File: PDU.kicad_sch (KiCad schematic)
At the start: 36 parts, among them Q37 PMOS, Q38 NPN, Q39 NPN, Q40 PMOS, Q41 NPN, Q42 PMOS, Q43 NPN, Q44 PMOS, Q45 NPN, Q46 PMOS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

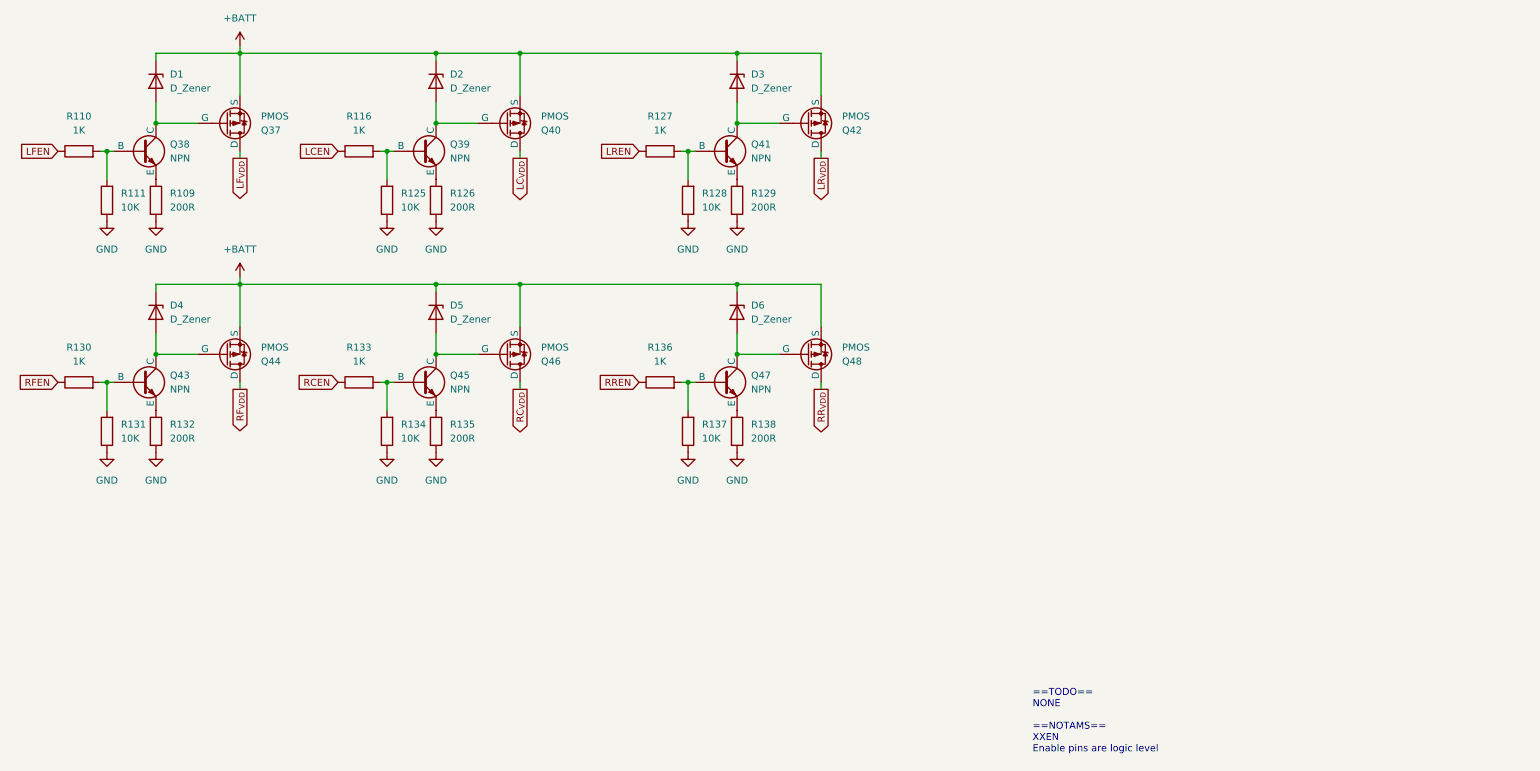
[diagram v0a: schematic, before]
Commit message: The great decluttering
Moved all possible controls to I2C, part selection commenced, IOs assigned pending comms schema
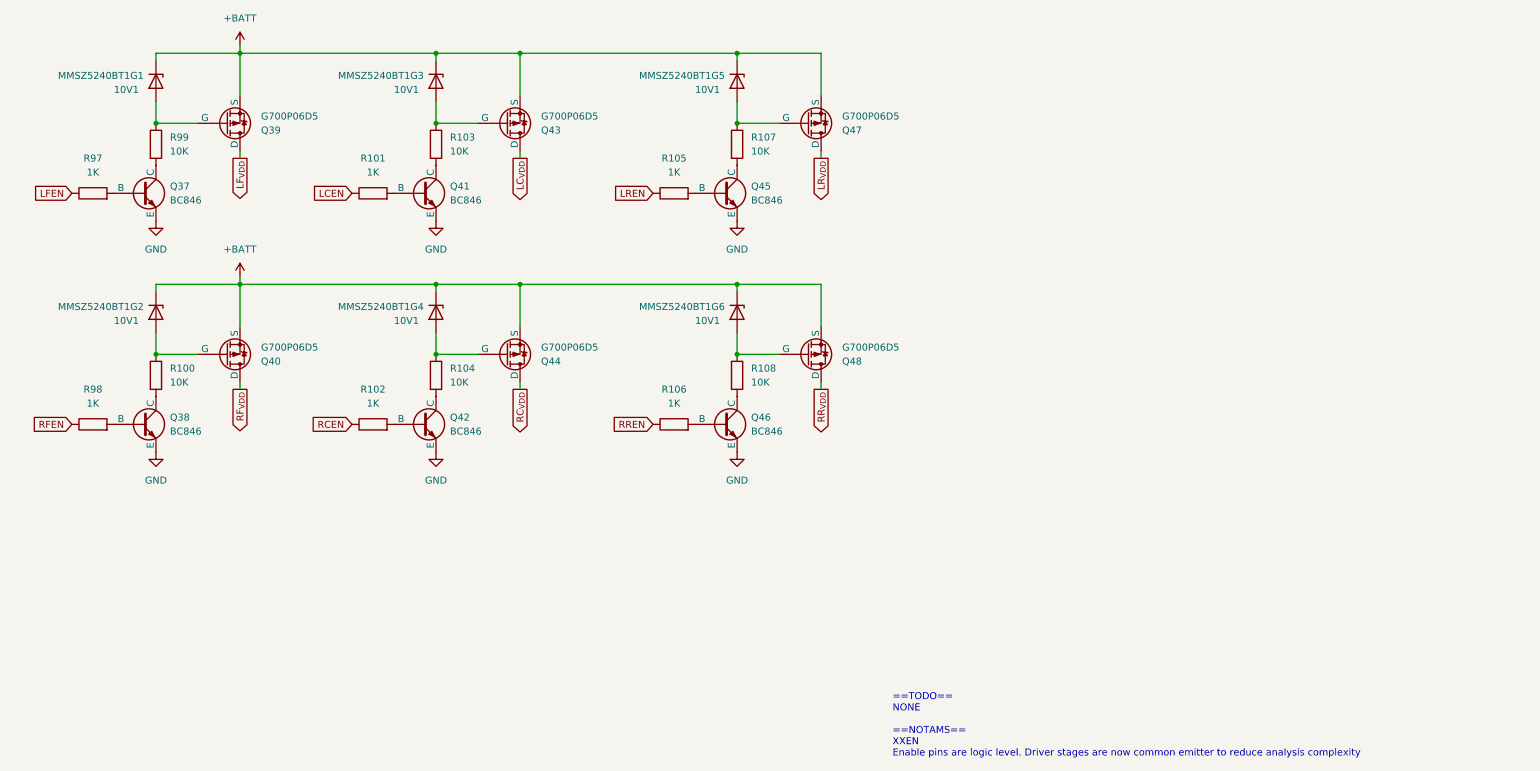
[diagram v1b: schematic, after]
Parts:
- removed D2, D3, D4, D5, D6: D_Zener, Diode_SMD:D_0603_1608Metric, symbol Device:D_Zener
- removed Q39, Q43, Q47: NPN, symbol Simulation_SPICE:NPN
- removed Q42, Q46: PMOS, symbol Simulation_SPICE:PMOS
- removed R109, R126, R129, R132, R135, R138: 200R, Resistor_SMD:R_0603_1608Metric, symbol Device:R
- removed R111, R125, R128, R131, R134, R137: 10K, Resistor_SMD:R_0603_1608Metric, symbol Device:R
- removed R116, R127, R130, R133, R136: 1K, Resistor_SMD:R_0603_1608Metric, symbol Device:R
- added MMSZ5240BT1G2, MMSZ5240BT1G3, MMSZ5240BT1G4, MMSZ5240BT1G5, MMSZ5240BT1G6: 10V1, Diode_SMD:D_SOD-123, symbol Device:D_Zener
- added Q38, Q42, Q46: BC846, Package_TO_SOT_SMD:SOT-23, symbol Simulation_SPICE:NPN
- added Q43, Q47: G700P06D5, Package_DFN_QFN:PQFN-8-EP_6x5mm_P1.27mm_Generic, symbol Simulation_SPICE:PMOS
- added R100, R103, R104, R107, R108, R99: 10K, Resistor_SMD:R_0603_1608Metric, symbol Device:R
- added R101, R102, R105, R106, R98: 1K, Resistor_SMD:R_0603_1608Metric, symbol Device:R
- MMSZ5240BT1G1: renamed from D1; value D_Zener -> 10V1; footprint Diode_SMD:D_0603_1608Metric -> Diode_SMD:D_SOD-123
- Q37: renamed from Q38; value NPN -> BC846; footprint (none) -> Package_TO_SOT_SMD:SOT-23
- Q39: renamed from Q37; value PMOS -> G700P06D5; footprint (none) -> Package_DFN_QFN:PQFN-8-EP_6x5mm_P1.27mm_Generic
- Q40, Q44, Q48: value PMOS -> G700P06D5; footprint (none) -> Package_DFN_QFN:PQFN-8-EP_6x5mm_P1.27mm_Generic
- Q41, Q45: value NPN -> BC846; footprint (none) -> Package_TO_SOT_SMD:SOT-23
- renumbered R110 to R97
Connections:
- net +BATT: now also MMSZ5240BT1G2.1 (K), MMSZ5240BT1G3.1 (K), MMSZ5240BT1G4.1 (K), MMSZ5240BT1G5.1 (K), MMSZ5240BT1G6.1 (K), Q43.3 (S), Q47.3 (S)
- net GND: now also Q37.3 (E), Q41.3 (E), Q45.3 (E), Q38.3 (E), Q42.3 (E), Q46.3 (E)
- net LCEN: now also R101.1
- net LC_{VDD}: now also Q43.1 (D); no longer Q40.1 (D)
- net LREN: now also R105.1
- net LR_{VDD}: now also Q47.1 (D)
- net RCEN: now also R102.1
- net RC_{VDD}: now also Q44.1 (D)
- net RFEN: now also R98.1
- net RF_{VDD}: now also Q40.1 (D); no longer Q44.1 (D)
- net RREN: now also R106.1
- net at Q40.2 (G): now also MMSZ5240BT1G2.2 (A), R100.1
- net at Q41.1 (C): now also R103.2
- net at Q41.2 (B): now also R101.2
- net at MMSZ5240BT1G1.2 (A), Q39.2 (G): now also R99.1; no longer Q37.1 (C)
- net at Q44.2 (G): now also MMSZ5240BT1G4.2 (A), R104.1
- net at Q45.1 (C): now also R107.2
- net at Q45.2 (B): now also R105.2
- net at Q48.2 (G): now also MMSZ5240BT1G6.2 (A), R108.1
- new net: MMSZ5240BT1G5.2 (A), Q47.2 (G), R107.1
- new net: Q37.1 (C), R99.2
- new net: Q38.1 (C), R100.2
- new net: Q38.2 (B), R98.2
- new net: Q42.2 (B), R102.2
- new net: MMSZ5240BT1G3.2 (A), Q43.2 (G), R103.1
- new net: Q42.1 (C), R104.2
- new net: Q46.1 (C), R108.2
- new net: Q46.2 (B), R106.2
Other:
- note added: "==TODO== NONE ==NOTAMS== XXEN Enable pins are logic level. Driver stages are now common emitter to reduce analysis complexity"
- note removed: "==TODO== NONE ==NOTAMS== XXEN Enable pins are logic level"
- moved on the sheet: Q37, R97

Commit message: Powerstage
Powerstage layout, non critical changes to schematic
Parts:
- removed Q39, Q40, Q43, Q44, Q47, Q48: G700P06D5, Package_DFN_QFN:PQFN-8-EP_6x5mm_P1.27mm_Generic, symbol Simulation_SPICE:PMOS
- added Q39, Q40, Q43, Q44, Q47, Q48: G700P06D5, Package_SO:PowerPAK_SO-8_Single, symbol Transistor_FET:CSD25402Q3A
- D1: renamed from MMSZ5240BT1G1; value 10V1 -> MMSZ5240BT1G5
- R100, R103, R104, R107, R108, R99: footprint Resistor_SMD:R_0603_1608Metric -> Resistor_SMD:R_1210_3225Metric
- R101, R102, R105, R106, R97, R98: footprint Resistor_SMD:R_0603_1608Metric -> Resistor_SMD:R_0201_0603Metric
- renumbered MMSZ5240BT1G2 to D2, MMSZ5240BT1G3 to D3, MMSZ5240BT1G4 to D4, MMSZ5240BT1G5 to D5, MMSZ5240BT1G6 to D6
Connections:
- net +BATT: now also Q39.5 (S), Q40.5 (S), Q43.5 (S), Q44.5 (S), Q47.5 (S), Q48.5 (S)
- net LC_{VDD}: now also Q43.1 (D), Q43.2 (D), Q43.3 (D)
- net LF_{VDD}: now also Q39.1 (D), Q39.2 (D), Q39.3 (D)
- net LR_{VDD}: now also Q47.1 (D), Q47.2 (D), Q47.3 (D)
- net RC_{VDD}: now also Q44.1 (D), Q44.2 (D), Q44.3 (D)
- net RF_{VDD}: now also Q40.1 (D), Q40.2 (D), Q40.3 (D)
- net RR_{VDD}: now also Q48.1 (D), Q48.2 (D), Q48.3 (D)
- net at D5.2 (A), R107.1: now also Q47.4 (G)
- net at D3.2 (A), R103.1: now also Q43.4 (G)
- net at D2.2 (A), R100.1: now also Q40.4 (G)
- net at D4.2 (A), R104.1: now also Q44.4 (G)
- net at D1.2 (A), R99.1: now also Q39.4 (G)
- net at D6.2 (A), R108.1: now also Q48.4 (G)
